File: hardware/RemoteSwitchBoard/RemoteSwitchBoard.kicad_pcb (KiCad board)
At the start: 2 copper layers, 64 x 47 mm, 52 parts, among them J1 Conn_Coaxial, J10 XT30PW-M, J2 Conn_01x05, J3 Conn_01x02, J4 Conn_01x02, J5 Conn_01x04, J6 Conn_01x04, J7 Conn_01x02, J8 Conn_01x05, J9 Conn_01x02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

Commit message: update
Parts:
- moved J1 2.64 mm to (125.8, 104.1)
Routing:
- net RF_SWCLK: track 35.5 -> 38.7 mm
- net Net-(J1-In): track 5.70 -> 8.32 mm
- net RF_BOOT: track 40.3 -> 41.2 mm
- net GND: vias 10 -> 48
- net (no net): vias 171 -> 0

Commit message: update
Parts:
- removed Y1: Crystal_GND2, Crystal:Resonator_SMD_Murata_CSTxExxV-3Pin_3.0x1.1mm_HandSoldering
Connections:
- U1 pad 2: Net-(U1-PF0) -> unconnected-(U1-PF0-Pad2)
- U1 pad 3: Net-(U1-PF1) -> unconnected-(U1-PF1-Pad3)
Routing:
- net +3.3V: track 136.5 -> 116.4 mm
- net Net-(U1-PF1): track 13.2 -> 0.00 mm
- net Net-(U1-PF0): track 9.89 -> 0.00 mm
- net Net-(BZ1-+): track 19.1 -> 18.2 mm

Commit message: update
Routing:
- net +3.3V: track 116.4 -> 129.3 mm
- net GND: vias 48 -> 55
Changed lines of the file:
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@@
-	)
-	(via
-		(at 92.475 105.73)
-		(size 0.8)
-		(drill 0.4)
-		(layers "F.Cu" "B.Cu")
-		(net 1)
 	)
 	(via
@@
 	)
 	(via
+		(at 120.77 105.05)
+		(size 0.8)
+		(drill 0.4)
+		(layers "F.Cu" "B.Cu")
+		(free yes)
+		(net 1)
+	)
+	(via
 		(at 100.16 98.45)
 		(size 0.8)
@@
 	)
 	(via
+		(at 84.55 110.43)
+		(size 0.8)
+		(drill 0.4)
+		(layers "F.Cu" "B.Cu")
+		(free yes)
+		(net 1)
+	)
+	(via
+		(at 121.8 102.94)
+		(size 0.8)
+		(drill 0.4)
+		(layers "F.Cu" "B.Cu")
+		(free yes)
+		(net 1)
+	)
+	(via
 		(at 116.2 117.075)
 		(size 0.8)
@@
 	)
 	(via
+		(at 120.97 102.87)
+		(size 0.8)
+		(drill 0.4)
+		(layers "F.Cu" "B.Cu")
+		(free yes)
+		(net 1)
+	)
+	(via
 		(at 119.09 104.96)
 		(size 0.8)
@@
 	)
 	(via
+		(at 121.59 105)
+		(size 0.8)
+		(drill 0.4)
+		(layers "F.Cu" "B.Cu")
+		(free yes)
+		(net 1)
+	)
+	(via
 		(at 85.76 120.66)
 		(size 0.8)
@@
 	)
 	(via
+		(at 102.06 115.26)
+		(size 0.8)
+		(drill 0.4)
+		(layers "F.Cu" "B.Cu")
+		(free yes)
+		(net 1)
+	)
+	(via
 		(at 71.09 83.71)
 		(size 0.8)
@@
 	)
 	(via
+		(at 122.56 105.08)
+		(size 0.8)
+		(drill 0.4)
+		(layers "F.Cu" "B.Cu")
+		(free yes)
+		(net 1)
+	)
+	(via
 		(at 72.3 100.8)
 		(size 0.8)
@@
 	(via
 		(at 65.62 106.39)
+		(size 0.8)
+		(drill 0.4)
+		(layers "F.Cu" "B.Cu")
+		(free yes)
+		(net 1)
+	)
+	(via
+		(at 122.71 102.93)
 		(size 0.8)
 		(drill 0.4)
@@
 	)
 	(segment
+		(start 103.248 97.793)
+		(end 103.1 97.645)
+		(width 0.4)
+		(layer "F.Cu")
+		(net 3)
+	)
+	(segment
 		(start 107.73 112.12)
 		(end 110.595 112.12)
@@
 	)
 	(segment
+		(start 100.075 109.15)
+		(end 103.248 105.977)
+		(width 0.4)
+		(layer "F.Cu")
+		(net 3)
+	)
+	(segment
 		(start 86.856786 98.274)
 		(end 85.37334 98.274)
@@
 		(width 0.4)
 		(layer "F.Cu")
+		(net 3)
+	)
+	(segment
+		(start 103.248 105.977)
+		(end 103.248 97.793)
+		(width 0.4)
+		(layer "F.Cu")

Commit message: update
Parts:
- moved R9 1.52 mm to (94.4, 116.3)
- moved D9 1.52 mm to (94.5, 114.7)
- moved R5 0.97 mm to (93.3, 108.2)
- moved R6 0.97 mm to (93.3, 105.1)
- moved R7 0.97 mm to (93.3, 113.0)
- moved D5 0.97 mm to (93.3, 109.7)
- moved D6 0.97 mm to (93.3, 106.7)
- moved D7 0.97 mm to (93.3, 111.4)
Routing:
- net LED_2: track 21.8 -> 24.4 mm
- net USART2_TX: track 37.3 -> 35.7 mm
- net LED_4: track 38.9 -> 40.2 mm

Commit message: update
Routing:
- net RF_SWDIO: track 39.0 -> 39.6 mm
- net GND: vias 55 -> 57
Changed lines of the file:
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@@
+	)
+	(via
+		(at 78.75 97.91)
+		(size 0.8)
+		(drill 0.4)
+		(layers "F.Cu" "B.Cu")
+		(free yes)
+		(net 1)
 	)
 	(via
@@
 	(via
 		(at 100.16 98.45)
+		(size 0.8)
+		(drill 0.4)
+		(layers "F.Cu" "B.Cu")
+		(free yes)
+		(net 1)
+	)
+	(via
+		(at 74.65 88.7)
 		(size 0.8)
 		(drill 0.4)
@@
 	)
 	(segment
-		(start 115.024 129.226)
-		(end 112.804306 129.226)
+		(start 112.79 129.64)
+		(end 111.71 128.56)
 		(width 0.25)
 		(layer "F.Cu")
@@
 	)
 	(segment
-		(start 112.174 127.944)
-		(end 103.774 119.544)
+		(start 114.61 129.64)
+		(end 112.79 129.64)
+		(width 0.25)
+		(layer "F.Cu")
+		(net 40)
+	)
+	(segment
+		(start 103.774 99.051)
+		(end 103.85 98.975)
+		(width 0.25)
+		(layer "F.Cu")
+		(net 40)
+	)
+	(segment
+		(start 111.71 128.56)
+		(end 111.71 127.75)
+		(width 0.25)
+		(layer "F.Cu")
+		(net 40)
+	)
+	(segment
+		(start 111.71 127.75)
+		(end 103.774 119.814)
 		(width 0.25)
 		(layer "F.Cu")
@@
 	)
 	(segment
-		(start 112.804306 129.226)
-		(end 112.174 128.595694)
+		(start 103.774 119.814)
+		(end 103.774 99.051)
 		(width 0.25)
 		(layer "F.Cu")
@@
 	)
 	(segment
-		(start 103.774 119.544)
-		(end 103.774 99.051)
-		(width 0.25)
-		(layer "F.Cu")
-		(net 40)
-	)
-	(segment
 		(start 116 128.25)
-		(end 115.024 129.226)
-		(width 0.25)
-		(layer "F.Cu")
-		(net 40)
-	)
-	(segment
-		(start 112.174 128.595694)
-		(end 112.174 127.944)
-		(width 0.25)
-		(layer "F.Cu")
-		(net 40)
-	)
-	(segment
-		(start 103.774 99.051)
-		(end 103.85 98.975)
-		(width 0.25)
-		(layer "F.Cu")
+		(end 114.61 129.64)
+		(width 0.25)
+		(layer "F.Cu")

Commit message: update
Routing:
- net GND: vias 57 -> 56
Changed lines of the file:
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@@
-	)
-	(via
-		(at 92.43 109.745)
-		(size 0.8)
-		(drill 0.4)
-		(layers "F.Cu" "B.Cu")
-		(net 1)
 	)
 	(via
@@
 	)
 	(segment
-		(start 103.248 97.793)
-		(end 103.1 97.645)
-		(width 0.4)
-		(layer "F.Cu")
-		(net 3)
-	)
-	(segment
 		(start 107.73 112.12)
 		(end 110.595 112.12)
@@
 	)
 	(segment
+		(start 103.06 97.685)
+		(end 103.1 97.645)
+		(width 0.4)
+		(layer "F.Cu")
+		(net 3)
+	)
+	(segment
 		(start 102.224 95.649001)
 		(end 103.1 96.525001)
@@
 	)
 	(segment
-		(start 100.075 109.15)
-		(end 103.248 105.977)
-		(width 0.4)
-		(layer "F.Cu")
-		(net 3)
-	)
-	(segment
 		(start 86.856786 98.274)
 		(end 85.37334 98.274)
@@
 	)
 	(segment
-		(start 103.248 105.977)
-		(end 103.248 97.793)
-		(width 0.4)
-		(layer "F.Cu")
-		(net 3)
-	)
-	(segment
 		(start 113.5 110.85)
 		(end 114.948999 109.401001)
@@
 	)
 	(segment
+		(start 100.075 109.15)
+		(end 103.06 106.165)
+		(width 0.4)
+		(layer "F.Cu")
+		(net 3)
+	)
+	(segment
 		(start 111.775 110.825)
 		(end 113.475 110.825)
 		(width 0.4)
 		(layer "F.Cu")
+		(net 3)
+	)
+	(segment
+		(start 103.06 106.165)
+		(end 103.06 97.685)
+		(width 0.4)
+		(layer "F.Cu")

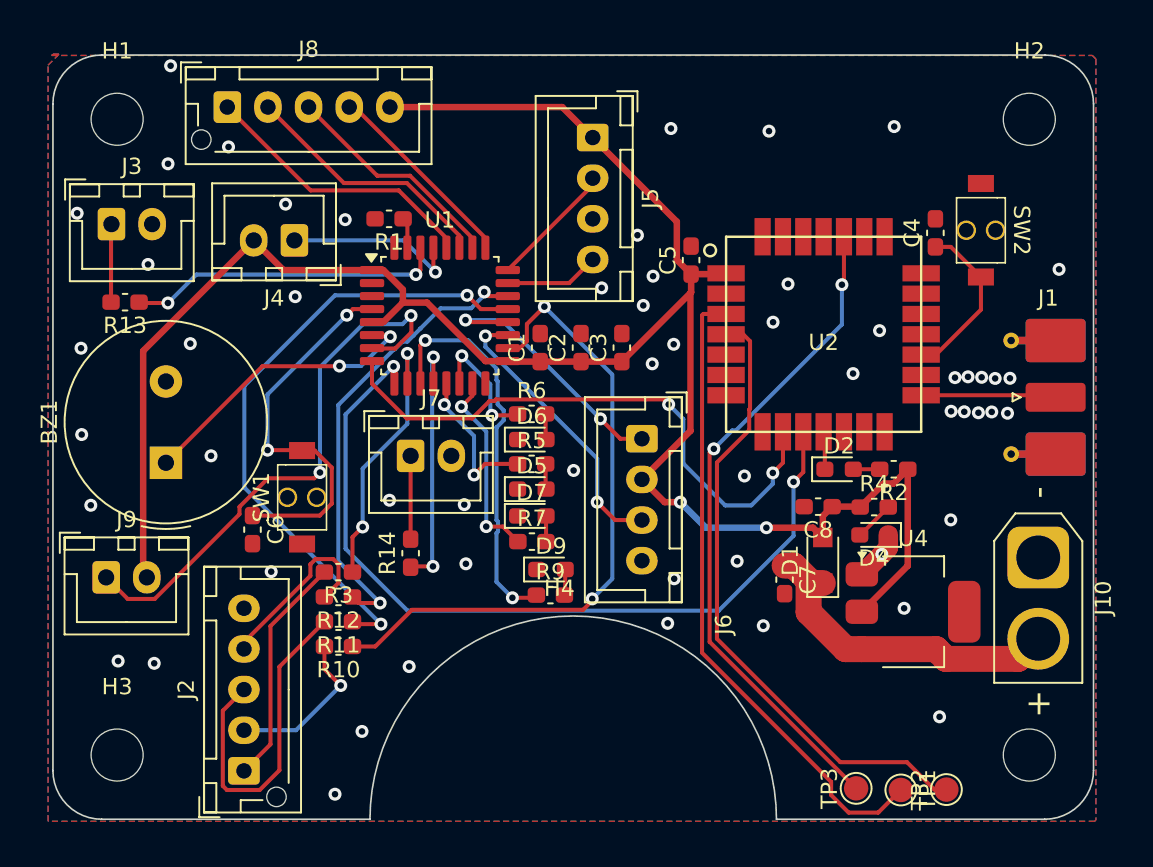
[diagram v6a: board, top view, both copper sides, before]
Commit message: update:配置の変更,配線の改善
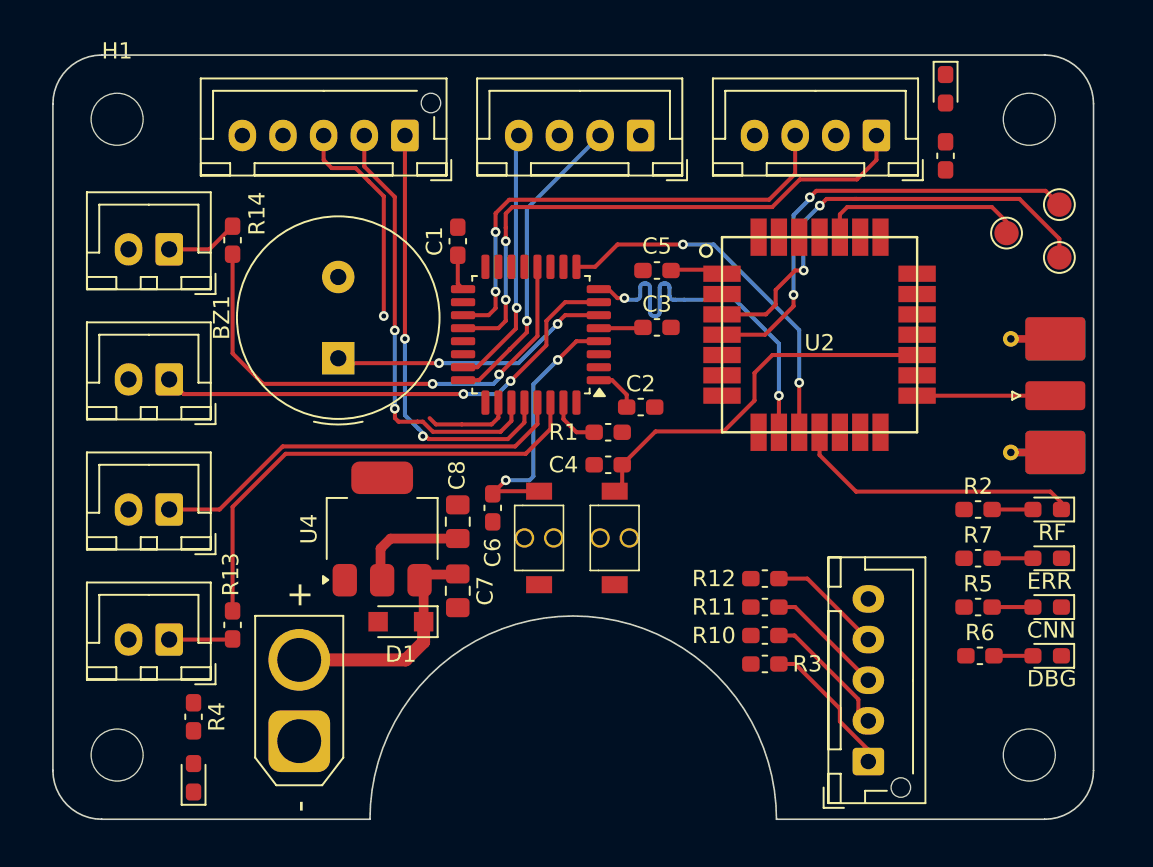
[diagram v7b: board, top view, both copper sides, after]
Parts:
- C7, C8: footprint Capacitor_SMD:C_0603_1608Metric_Pad1.08x0.95mm_HandSolder -> Capacitor_SMD:C_0805_2012Metric_Pad1.18x1.45mm_HandSolder
- moved J10 46.8 mm to (79.0, 125.2), turned to 90 degrees
- moved D4 44.4 mm to (72.5, 127.5), turned to 90 degrees
- moved R4 43.8 mm to (72.5, 123.8), turned to -90 degrees
- moved J2 38.4 mm to (114.0, 126.5)
- moved D9 38.2 mm to (118.8, 85.1), turned to -90 degrees
- moved TP2 36.6 mm to (125.8, 92.2), turned to 180 degrees
- moved R9 36.3 mm to (118.8, 89.2), turned to -90 degrees
- moved TP3 35.4 mm to (122.5, 94.0), turned to 180 degrees
- moved D6 34.4 mm to (125.0, 120.0), turned to 180 degrees
- moved TP1 34.2 mm to (125.8, 95.5), turned to 0 degrees
- moved U4 33.0 mm to (84.1, 112.2), turned to 90 degrees
- moved D5 32.5 mm to (125.0, 117.0), turned to 180 degrees
- moved D7 31.8 mm to (125.0, 114.0), turned to 180 degrees
- moved R6 31.3 mm to (120.9, 120.0)
- moved SW2 29.4 mm to (98.4, 112.8), turned to 90 degrees
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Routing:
- net +3.3V: track 129.1 -> 17.7 mm, vias 2 -> 0
- net LED_4: track 40.2 -> 0.00 mm, vias 2 -> 0
- net LED_5: track 38.8 -> 0.00 mm, vias 2 -> 0
- net LED_6: track 28.6 -> 0.00 mm, vias 2 -> 0
- net USART2_RX: track 51.2 -> 22.7 mm
- net RF_BOOT: track 41.2 -> 12.9 mm, vias 2 -> 0
- net LED_2: track 24.4 -> 0.00 mm, vias 2 -> 0
- net USART1_RX: track 16.5 -> 35.1 mm
- net LED_3: track 16.7 -> 0.00 mm, vias 2 -> 0
- net RF_LED: track 2.33 -> 17.9 mm
- net LED_1: track 15.9 -> 31.2 mm
- net bustop: track 11.0 -> 26.1 mm, vias 1 -> 0
- net RF_RST: track 10.4 -> 24.0 mm
- net Net-(J2-Pin_3): track 20.8 -> 7.36 mm
- net USART2_TX: track 35.7 -> 23.0 mm
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- removed copper zone on B.Cu, net GND
- removed copper zone on F.Cu, net GND
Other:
- copper layers 2 -> 4
- board text added: "CNN"
- board text added: "DBG"
- board text added: "ERR"
- board text added: "RF"

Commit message: add:gaber
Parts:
- removed D5, D6, D7, D9: LED, LED_SMD:LED_0603_1608Metric_Pad1.05x0.95mm_HandSolder
- removed J4: Conn_01x02, Connector_JST:JST_XH_B2B-XH-A_1x02_P2.50mm_Vertical
- removed J8: Conn_01x05, Connector_JST:JST_XH_B5B-XH-AM_1x05_P2.50mm_Vertical
- removed R5, R6, R7, R9: 1k, Capacitor_SMD:C_0603_1608Metric_Pad1.08x0.95mm_HandSolder
- removed TP1, TP2, TP3: TestPoint, TestPoint:TestPoint_Pad_D1.5mm
- added SW3: SW_DIP_x04, Button_Switch_SMD:SW_DIP_SPSTx04_Slide_Copal_CHS-04B_W7.62mm_P1.27mm, F.Cu at (69.7, 110.1)
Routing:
- net +3.3V: track 17.7 -> 184.8 mm, vias 0 -> 3
- net LED_4: track 0.00 -> 43.9 mm, vias 0 -> 2
- net LED_5: track 0.00 -> 41.2 mm, vias 0 -> 2
- net LED_6: track 0.00 -> 38.9 mm, vias 0 -> 2
- net LED_3: track 0.00 -> 31.3 mm, vias 0 -> 2
- net RF_SWDIO: track 28.4 -> 0.00 mm, vias 2 -> 0
- net RF_SWCLK: track 28.2 -> 0.00 mm, vias 2 -> 0
- net bustop: track 26.1 -> 0.00 mm
- net DIP_4: track 0.00 -> 19.0 mm
- net RF_BOOT: track 12.9 -> 0.00 mm
- net GND: track 0.00 -> 7.12 mm, vias 0 -> 98
- net DIP_2: track 27.1 -> 22.3 mm, vias 2 -> 0
- net DIP_1: track 26.9 -> 24.2 mm, vias 2 -> 0
- net Net-(D7-A): track 2.51 -> 0.00 mm
- net Net-(D5-A): track 2.51 -> 0.00 mm
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- added copper zone on B.Cu, net GND
- added copper zone on F.Cu, net GND
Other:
- copper layers 4 -> 2
- board text removed: "CNN"
- board text removed: "DBG"
- board text removed: "ERR"
